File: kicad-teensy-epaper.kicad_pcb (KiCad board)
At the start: 2 copper layers, 110.4 x 57.2 mm, 18 parts, among them J1 TEENSY3.2-72MHz, J2 HEADER-FEMALE-34POS-FFC-SMT-1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, Q1 Q_NMOS_GDS

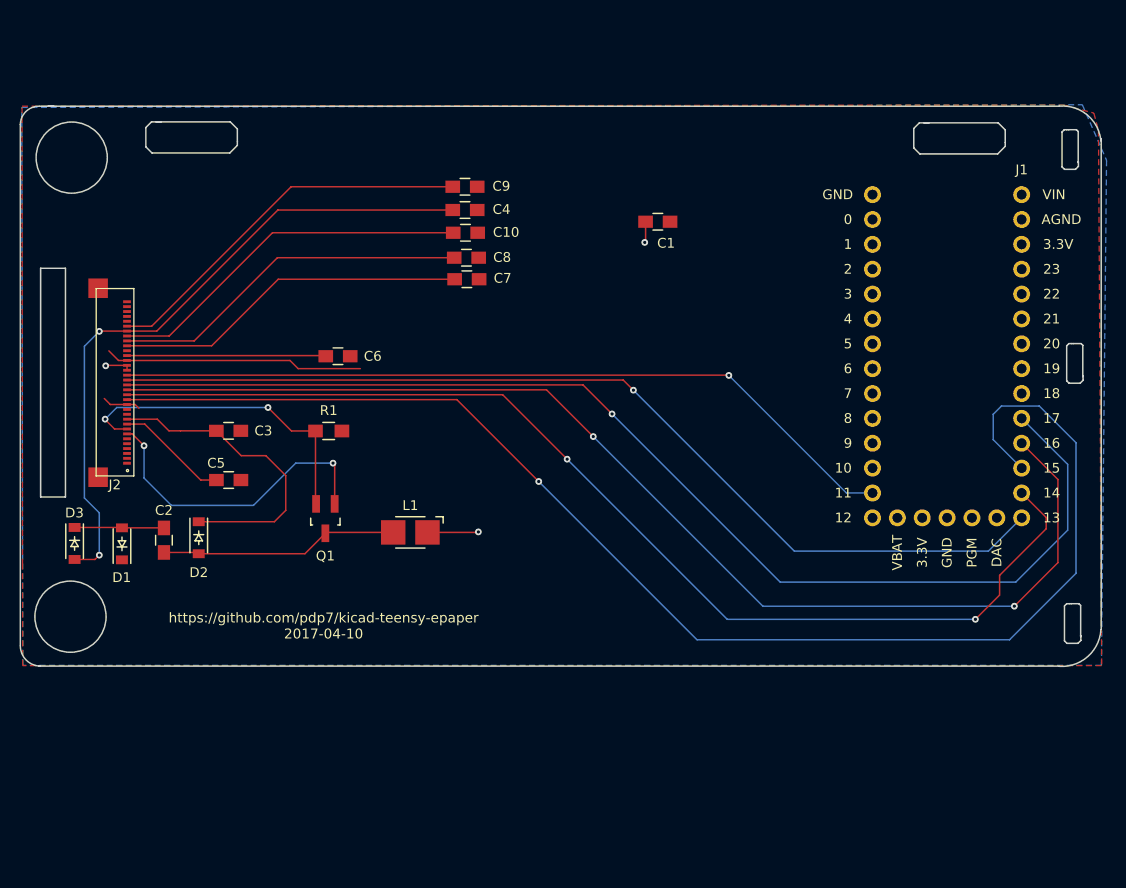
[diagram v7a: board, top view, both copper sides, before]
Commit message: redesigned for smaller size and cap touch
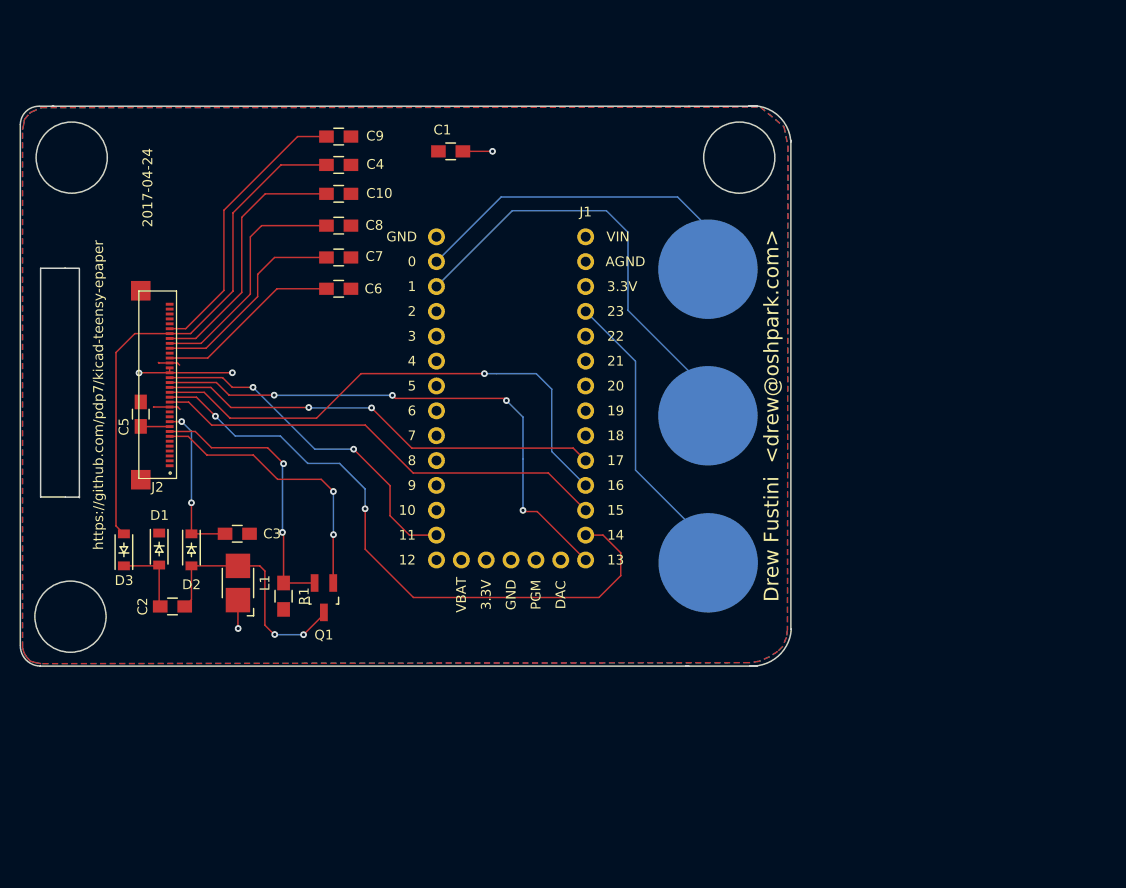
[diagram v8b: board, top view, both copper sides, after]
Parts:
- added A: CAPSENSE_CIRCLE, Wickerlib:CAPSENSE-CIRCLE-D10MM, B.Cu at (135.0, 78.8)
- added CAP1: CAPSENSE_CIRCLE, Wickerlib:CAPSENSE-CIRCLE-D10MM, B.Cu at (135.0, 48.8)
- added CAP2: CAPSENSE_CIRCLE, Wickerlib:CAPSENSE-CIRCLE-D10MM, B.Cu at (135.0, 63.8)
- moved J1 44.8 mm to (117.4, 55.6)
- moved C1 22.4 mm to (108.7, 36.7), turned to 0 degrees
- moved L1 18.4 mm to (87.0, 80.8), turned to 90 degrees
- moved R1 17.5 mm to (91.7, 82.2), turned to 270 degrees
- moved C9 13.9 mm to (97.3, 35.2)
- moved C4 13.7 mm to (97.3, 38.1)
- moved C10 13.6 mm to (97.3, 41.1)
- moved C8 13.5 mm to (97.3, 44.3)
- moved C7 13.3 mm to (97.3, 47.6)
- moved C5 11.2 mm to (77.1, 63.6), turned to 270 degrees
- moved C3 10.6 mm to (86.9, 75.8)
- moved Q1 8.08 mm to (95.8, 82.3)
- moved C6 6.89 mm to (97.3, 50.8)
- moved C2 6.82 mm to (80.3, 83.2), turned to 0 degrees
- moved D3 5.08 mm to (75.4, 77.4), turned to 90 degrees
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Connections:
- net VPP renamed Net-(J2-Pad24)
- J1 pad 3V2: Net-(J1-Pad3V2) -> VDDIO
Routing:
- net BUSY: track 140.6 -> 47.1 mm, vias 1 -> 0
- net ^CS: track 120.0 -> 45.6 mm, vias 1 -> 2
- net ^D/C: track 119.8 -> 53.9 mm, vias 2 -> 1
- net Net-(CAP2-Pad1): track 0.00 -> 48.0 mm
- net ^RES: track 113.1 -> 65.8 mm
- net DOUT: track 81.1 -> 35.7 mm, vias 1 -> 2
- net SCK: track 100.0 -> 55.6 mm, vias 1 -> 4
- net Net-(CAP1-Pad1): track 0.00 -> 36.0 mm
- net Net-(CAP3-Pad1): track 0.00 -> 30.9 mm
- net GND: track 30.4 -> 5.11 mm
- net PRVGL: track 68.1 -> 53.0 mm, vias 2 -> 0
- net VSH: track 36.3 -> 21.2 mm
- net VGH: track 31.5 -> 16.6 mm, vias 0 -> 2
- net VGH2: track 36.9 -> 24.4 mm
- net VSL: track 37.7 -> 26.6 mm
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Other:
- board size 110.4 x 57.2 mm -> 78.8 x 57.3 mm
- board text added: "2017-04-24"
- board text added: "Drew Fustini <drew@oshpark.com>"
- board text added: "https://github.com/pdp7/kicad-teensy-epaper"
- board text removed: "Drew Fustini drew@oshpark.com"
- board text removed: "github.com/pdp7/kicad-teensy-epaper"
- board text removed: "https://github.com/pdp7/kicad-teensy-epaper 2017-04-10"
